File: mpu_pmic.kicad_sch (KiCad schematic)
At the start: 48 parts, among them U501 STPMIC1DPQR

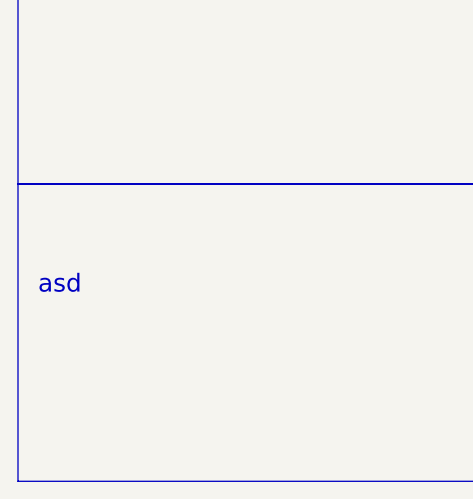
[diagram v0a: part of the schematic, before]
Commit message: Add MPU boot selection
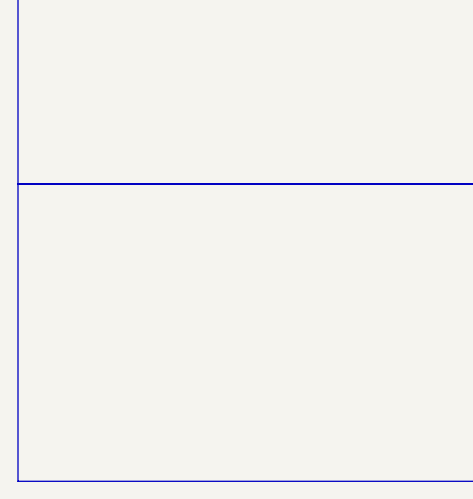
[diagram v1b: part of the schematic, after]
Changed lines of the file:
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@@
-		)
-	)
-	(text_box "asd"
-		(exclude_from_sim no)
-		(at 13.97 260.35 0)
-		(size 283.21 22.86)
-		(margins 0.9525 0.9525 0.9525 0.9525)
-		(stroke
-			(width -0.0001)
-			(type solid)
-		)
-		(fill
-			(type none)
-		)
-		(effects
-			(font
-				(size 2 2)
-			)
-			(justify left top)
 		)
 	)

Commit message: Add a debug section
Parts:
- added R501: 10 kΩ, perfect_footprints:R_0402_1005Metric, symbol Device:R
- renumbered R501 to R502, R502 to R503
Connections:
- net RST_N: now also R501.2
- net V_3V3: now also R501.1
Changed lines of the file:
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@@
 	)
 	(junction
+		(at 97.79 200.66)
+		(diameter 0)
+		(color 0 0 0 0)
+	)
+	(junction
 		(at 349.25 152.4)
 		(diameter 0)
@@
 	)
 	(junction
+		(at 97.79 176.53)
+		(diameter 0)
+		(color 0 0 0 0)
+	)
+	(junction
 		(at 142.24 149.86)
 		(diameter 0)
@@
 	)
 	(bus_entry
-		(at 99.06 203.2)
+		(at 91.44 203.2)
 		(size -2.54 -2.54)
 		(stroke
@@
 	)
 	(bus_entry
-		(at 99.06 195.58)
+		(at 91.44 195.58)
 		(size -2.54 -2.54)
 		(stroke
@@
 	)
 	(bus_entry
-		(at 99.06 205.74)
+		(at 91.44 205.74)
 		(size -2.54 -2.54)
 		(stroke
@@
 	)
 	(bus_entry
-		(at 99.06 193.04)
+		(at 91.44 193.04)
 		(size -2.54 -2.54)
 		(stroke
@@
 	)
 	(bus_entry
-		(at 99.06 200.66)
+		(at 91.44 200.66)
 		(size -2.54 -2.54)
 		(stroke
@@
 	)
 	(bus_entry
-		(at 99.06 198.12)
+		(at 91.44 198.12)
 		(size -2.54 -2.54)
 		(stroke
@@
 	(wire
 		(pts
-			(xy 102.87 176.53) (xy 109.22 176.53)
+			(xy 88.9 176.53) (xy 97.79 176.53)
 		)
 		(stroke
@@
 	(wire
 		(pts
+			(xy 97.79 176.53) (xy 109.22 176.53)
+		)
+		(stroke
+			(width 0)
+			(type default)
+		)
+	)
+	(wire
+		(pts
 			(xy 116.84 125.73) (xy 104.14 125.73)
 		)
@@
 	(bus
 		(pts
-			(xy 95.25 190.5) (xy 96.52 190.5)
+			(xy 87.63 190.5) (xy 88.9 190.5)
 		)
 		(stroke
@@
 	(wire
 		(pts
-			(xy 99.06 198.12) (xy 124.46 198.12)
+			(xy 91.44 198.12) (xy 124.46 198.12)
 		)
 		(stroke
@@
 	(wire
 		(pts
-			(xy 99.06 195.58) (xy 109.22 195.58)
+			(xy 91.44 195.58) (xy 109.22 195.58)
 		)
 		(stroke
@@
 	(wire
 		(pts
+			(xy 97.79 176.53) (xy 97.79 179.07)
+		)
+		(stroke
+			(width 0)
+			(type default)
+		)
+	)
+	(wire
+		(pts
 			(xy 109.22 176.53) (xy 121.92 176.53)
 		)
@@
 	(wire
 		(pts
-			(xy 99.06 205.74) (xy 101.6 205.74)
+			(xy 91.44 205.74) (xy 101.6 205.74)
 		)
 		(stroke
@@
 	(bus
 		(pts
-			(xy 96.52 198.12) (xy 96.52 195.58)
+			(xy 88.9 198.12) (xy 88.9 195.58)
 		)
 		(stroke
@@
 	(bus
 		(pts
-			(xy 96.52 200.66) (xy 96.52 198.12)
+			(xy 88.9 200.66) (xy 88.9 198.12)
 		)
 		(stroke
@@
 	(bus
 		(pts
-			(xy 96.52 193.04) (xy 96.52 195.58)
+			(xy 88.9 193.04) (xy 88.9 195.58)
 		)
 		(stroke
@@
 	(wire
 		(pts
-			(xy 99.06 200.66) (xy 116.84 200.66)
+			(xy 91.44 200.66) (xy 97.79 200.66)
 		)
 		(stroke
@@
 	(bus
 		(pts
-			(xy 96.52 203.2) (xy 96.52 200.66)
+			(xy 88.9 203.2) (xy 88.9 200.66)
 		)
 		(stroke
@@
 	(bus
 		(pts
-			(xy 96.52 193.04) (xy 96.52 190.5)
+			(xy 88.9 193.04) (xy 88.9 190.5)
 		)
 		(stroke
@@
 	(wire
 		(pts
-			(xy 99.06 203.2) (xy 109.22 203.2)
+			(xy 91.44 203.2) (xy 109.22 203.2)
 		)
 		(stroke
@@
 	(wire
 		(pts
-			(xy 99.06 193.04) (xy 121.92 193.04)
+			(xy 91.44 193.04) (xy 121.92 193.04)
 		)
 		(stroke
@@
 	(wire
 		(pts
+			(xy 97.79 200.66) (xy 116.84 200.66)
+		)
+		(stroke
+			(width 0)
+			(type default)
+		)
+	)
+	(wire
+		(pts
 			(xy 336.55 240.03) (xy 339.09 240.03)
 		)
@@
 	(wire
 		(pts
+			(xy 97.79 186.69) (xy 97.79 200.66)
+		)
+		(stroke
+			(width 0)
+			(type default)
+		)
+	)
+	(wire
+		(pts
 			(xy 302.26 166.37) (xy 302.26 165.1)
 		)
@@
 	(hierarchical_label "V_3V3"
 		(shape input)
-		(at 102.87 176.53 180)
+		(at 88.9 176.53 180)
 		(effects
 			(font
@@
 	(hierarchical_label "{PMIC}"
 		(shape bidirectional)
-		(at 95.25 190.5 180)
+		(at 87.63 190.5 180)
 		(effects
 			(font
@@
 		(on_board yes)
 		(dnp no)
-		(property "Reference" "R502"
+		(property "Reference" "R503"
 			(at 124.46 181.6099 0)
 			(effects
@@
 			(project "linux-sbc"
 				(path "/fa11a02f-8043-4153-ab69-88d766503017/2d01087b-54dc-4f43-9cc7-a0ba17201776/8c2fc621-bdce-4f4c-8cac-9098b808a2b8"
-					(reference "R502")
+					(reference "R503")
 					(unit 1)
 				)
@@
 	)
 	(symbol
+		(lib_id "Device:R")
+		(at 97.79 182.88 0)
+		(unit 1)
+		(exclude_from_sim no)
+		(in_bom yes)
+		(on_board yes)
+		(dnp no)
+		(property "Reference" "R501"
+			(at 100.33 181.6099 0)
+			(effects
+				(font
+					(size 1.27 1.27)
+				)
+				(justify left)
+			)
+		)
+		(property "Value" "10 kΩ"
+			(at 100.33 184.1499 0)
+			(effects
+				(font
+					(size 1.27 1.27)
+				)
+				(justify left)
+			)
+		)
+		(property "Footprint" "perfect_footprints:R_0402_1005Metric"
+			(at 96.012 182.88 90)
+			(effects
+				(font
+					(size 1.27 1.27)
+				)
+				(hide yes)
+			)
+		)
+		(property "Datasheet" "https://www.we-online.com/components/products/datasheet/560112110020.pdf"
+			(at 97.79 182.88 0)
+			(effects
+				(font
+					(size 1.27 1.27)
+				)
+				(hide yes)
+			)
+		)
+		(property "Description" "Resistor"
+			(at 97.79 182.88 0)
+			(effects
+				(font
+					(size 1.27 1.27)
+				)
+				(hide yes)
+			)
+		)
+		(property "DigiKey Part Number" "732-560112110020CT-ND"
+			(at 97.79 182.88 0)
+			(effects
+				(font
+					(size 1.27 1.27)
+				)
+				(hide yes)
+			)
+		)
+		(property "MPN" "560112110020"
+			(at 97.79 182.88 0)
+			(effects
+				(font
+					(size 1.27 1.27)
+				)
+				(hide yes)
+			)
+		)
+		(property "Manufacturer" "Würth Elektronik"
+			(at 97.79 182.88 0)
+			(effects
+				(font
+					(size 1.27 1.27)
+				)
+				(hide yes)
+			)
+		)
+		(property "Temperature Coefficient" ""
+			(at 97.79 182.88 0)
+			(effects
+				(font
+					(size 1.27 1.27)
+				)
+				(hide yes)
+			)
+		)
+		(pin "2"
+		)
+		(pin "1"
+		)
+		(instances
+			(project "linux-sbc"
+				(path "/fa11a02f-8043-4153-ab69-88d766503017/2d01087b-54dc-4f43-9cc7-a0ba17201776/8c2fc621-bdce-4f4c-8cac-9098b808a2b8"
+					(reference "R501")
+					(unit 1)
+				)
+			)
+		)
+	)
+	(symbol
 		(lib_id "STMicroelectronics:STPMIC1DPQR")
 		(at 182.88 160.02 0)
@@
 		(on_board yes)
 		(dnp no)
-		(property "Reference" "R501"
+		(property "Reference" "R502"
 			(at 111.76 181.6099 0)
 			(effects
@@
 			(project "linux-sbc"
 				(path "/fa11a02f-8043-4153-ab69-88d766503017/2d01087b-54dc-4f43-9cc7-a0ba17201776/8c2fc621-bdce-4f4c-8cac-9098b808a2b8"
-					(reference "R501")
+					(reference "R502")
 					(unit 1)
 				)

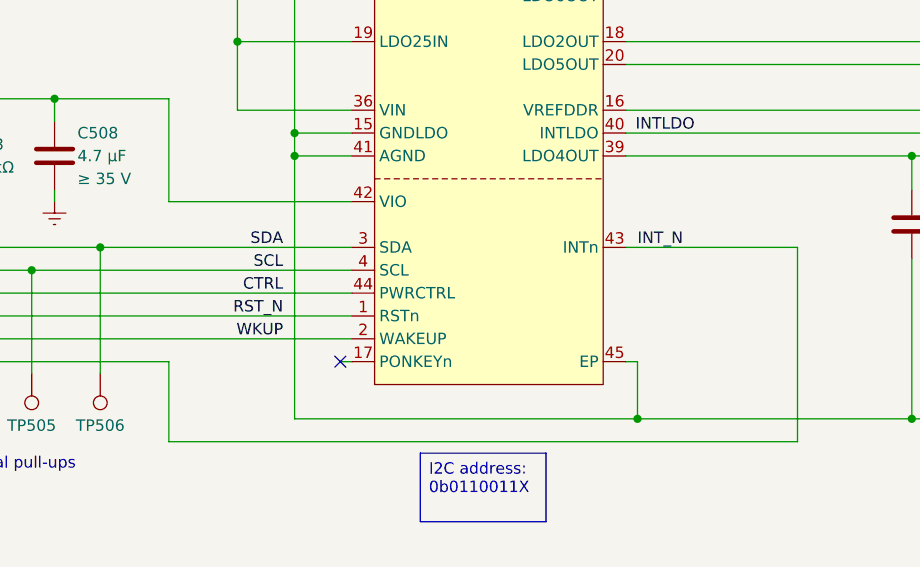
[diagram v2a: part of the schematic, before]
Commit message: Add ETH schema
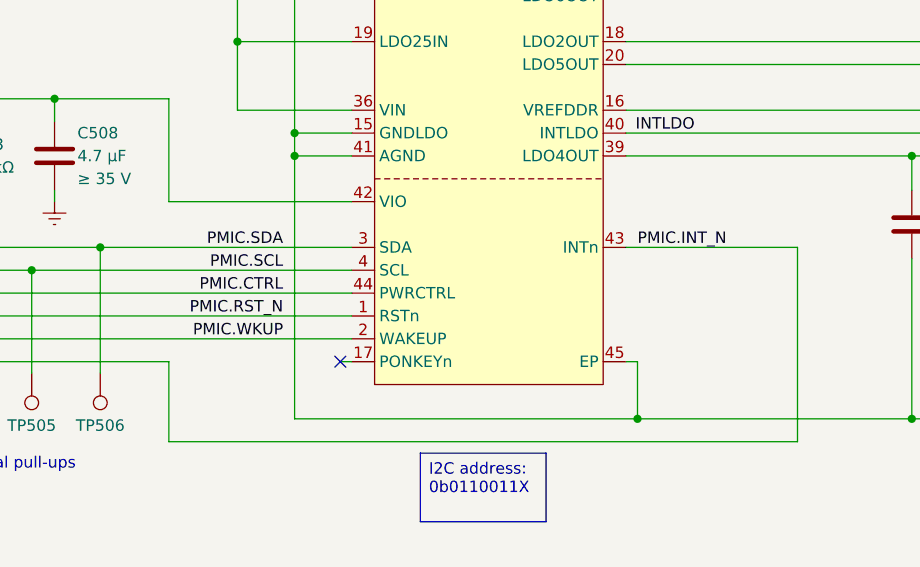
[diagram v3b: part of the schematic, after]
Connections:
- net CTRL renamed PMIC.CTRL
- net INT_N renamed PMIC.INT_N
- net RST_N renamed PMIC.RST_N
- net SCL renamed PMIC.SCL
- net SDA renamed PMIC.SDA
- net WKUP renamed PMIC.WKUP
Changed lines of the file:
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@@
 	)
 	(bus_alias "PMIC"
-		(members "SDA" "SCL" "CTRL" "RST_N" "WKUP" "INT_N")
+		(members "PMIC.SDA" "PMIC.SCL" "PMIC.CTRL" "PMIC.RST_N" "PMIC.WKUP" "PMIC.INT_N")
 	)
 	(text "RST_N & INT_N have internal pull-ups"
@@
 		)
 	)
-	(label "SCL"
+	(label "PMIC.SCL"
 		(at 160.02 195.58 180)
 		(effects
@@
 		)
 	)
-	(label "INT_N"
+	(label "PMIC.INT_N"
 		(at 199.39 193.04 0)
 		(effects
@@
 		)
 	)
-	(label "SDA"
+	(label "PMIC.SDA"
 		(at 160.02 193.04 180)
 		(effects
@@
 		)
 	)
-	(label "CTRL"
+	(label "PMIC.CTRL"
 		(at 160.02 198.12 180)
 		(effects
@@
 		)
 	)
-	(label "WKUP"
+	(label "PMIC.WKUP"
 		(at 160.02 203.2 180)
 		(effects
@@
 		)
 	)
-	(label "RST_N"
+	(label "PMIC.RST_N"
 		(at 160.02 200.66 180)
 		(effects

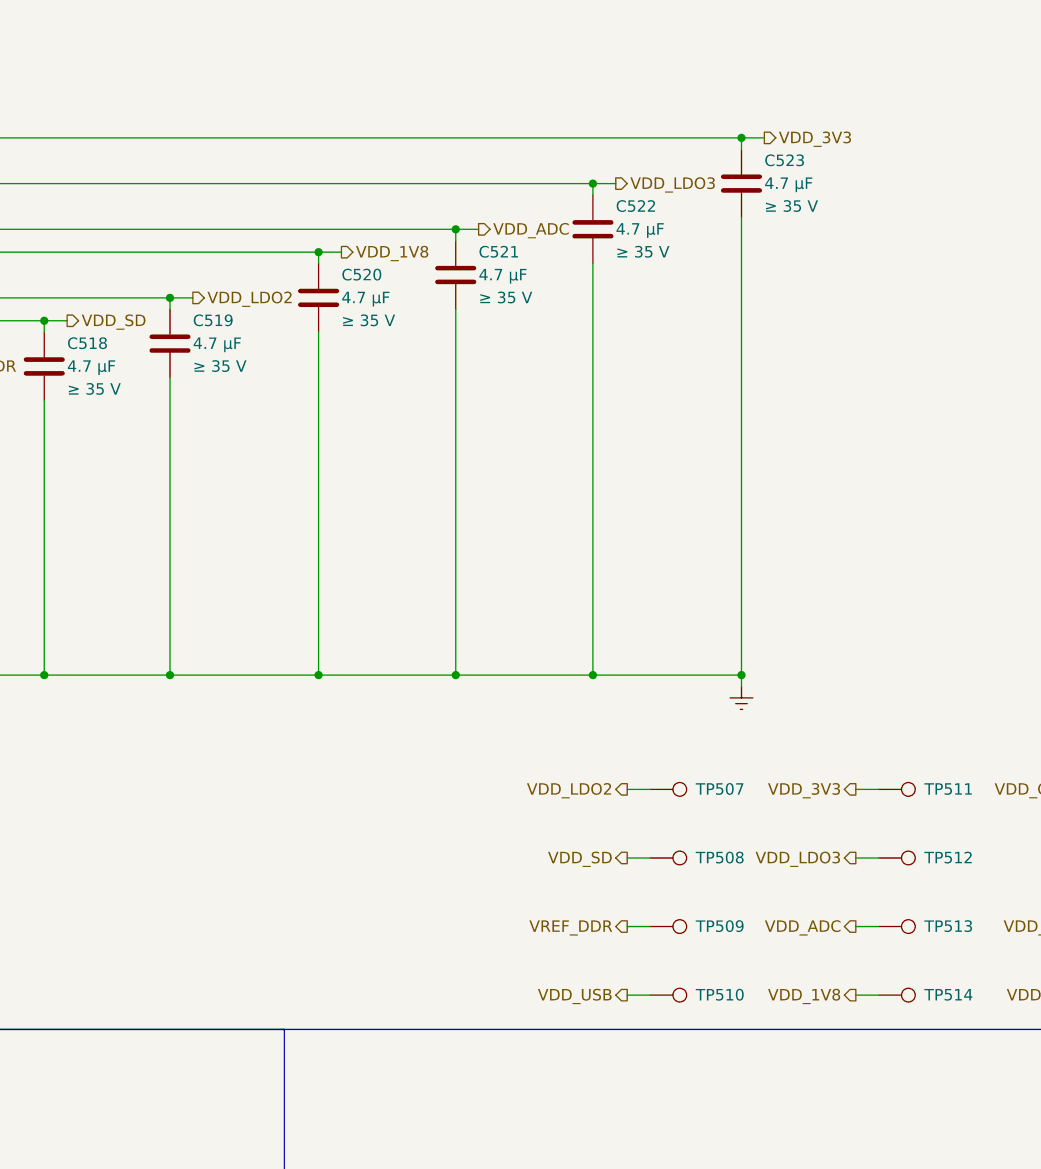
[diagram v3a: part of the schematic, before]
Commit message: Add LCD screen
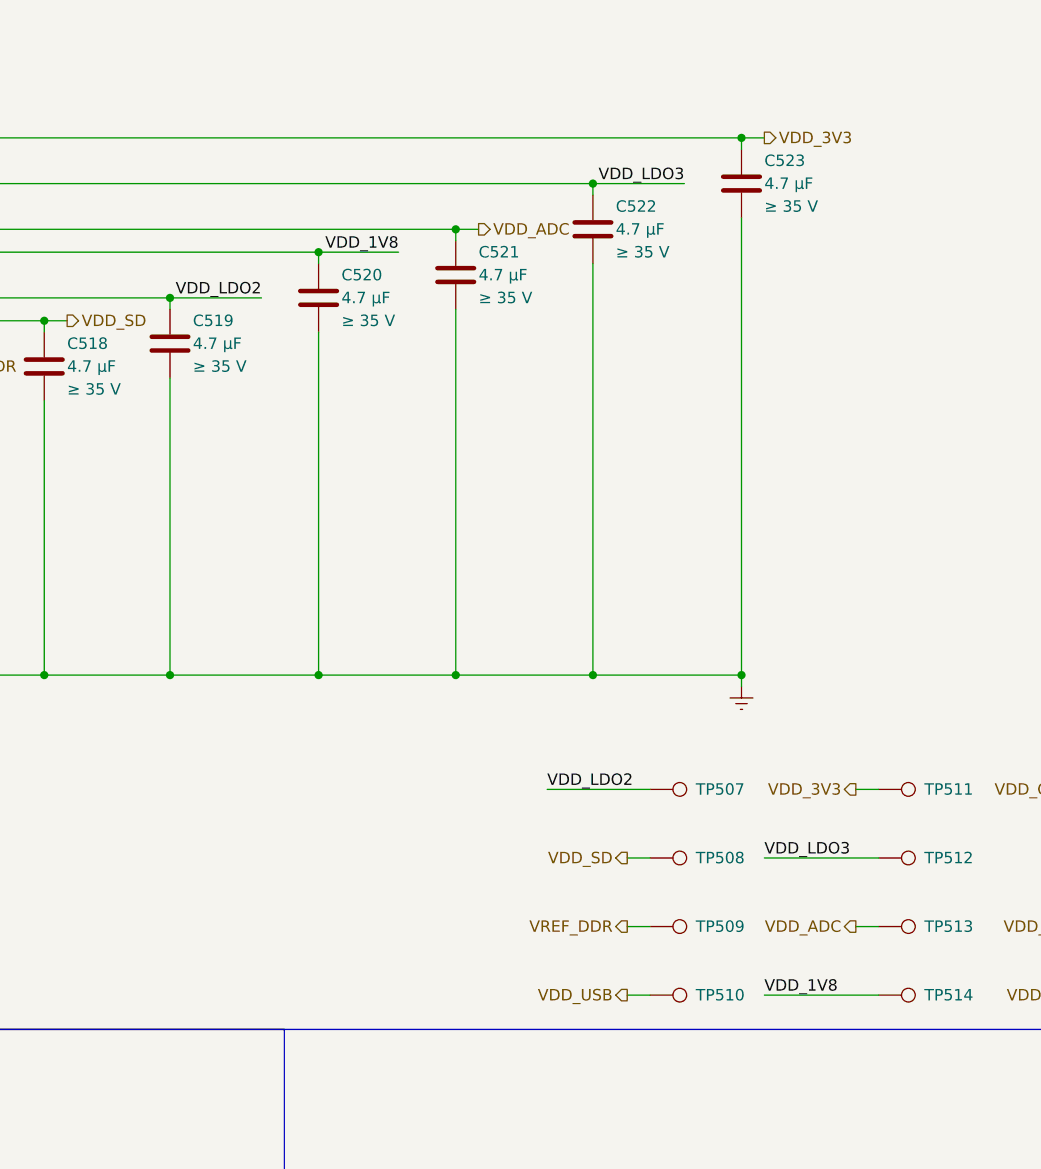
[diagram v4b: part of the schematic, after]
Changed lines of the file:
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@@
 	(wire
 		(pts
-			(xy 285.75 170.18) (xy 288.29 170.18)
+			(xy 285.75 170.18) (xy 295.91 170.18)
 		)
 		(stroke
@@
 	(wire
 		(pts
-			(xy 332.74 157.48) (xy 335.28 157.48)
+			(xy 332.74 157.48) (xy 342.9 157.48)
 		)
 		(stroke
@@
 	(wire
 		(pts
-			(xy 302.26 165.1) (xy 304.8 165.1)
+			(xy 302.26 165.1) (xy 311.15 165.1)
 		)
 		(stroke
@@
 	(wire
 		(pts
-			(xy 361.95 232.41) (xy 364.49 232.41)
+			(xy 351.79 232.41) (xy 364.49 232.41)
 		)
 		(stroke
@@
 	(wire
 		(pts
-			(xy 336.55 224.79) (xy 339.09 224.79)
+			(xy 327.66 224.79) (xy 339.09 224.79)
 		)
 		(stroke
@@
 	(wire
 		(pts
-			(xy 361.95 247.65) (xy 364.49 247.65)
+			(xy 351.79 247.65) (xy 364.49 247.65)
 		)
 		(stroke
@@
 			(width 0)
 			(type default)
+		)
+	)
+	(label "VDD_LDO3"
+		(at 342.9 157.48 180)
+		(effects
+			(font
+				(size 1.27 1.27)
+			)
+			(justify right bottom)
+		)
+	)
+	(label "VDD_1V8"
+		(at 351.79 247.65 0)
+		(effects
+			(font
+				(size 1.27 1.27)
+			)
+			(justify left bottom)
+		)
+	)
+	(label "VDD_1V8"
+		(at 311.15 165.1 180)
+		(effects
+			(font
+				(size 1.27 1.27)
+			)
+			(justify right bottom)
+		)
+	)
+	(label "VDD_LDO3"
+		(at 351.79 232.41 0)
+		(effects
+			(font
+				(size 1.27 1.27)
+			)
+			(justify left bottom)
 		)
 	)
@@
 		)
 	)
+	(label "VDD_LDO2"
+		(at 295.91 170.18 180)
+		(effects
+			(font
+				(size 1.27 1.27)
+			)
+			(justify right bottom)
+		)
+	)
 	(label "PMIC.SDA"
 		(at 160.02 193.04 180)
@@
 		)
 	)
+	(label "VDD_LDO2"
+		(at 327.66 224.79 0)
+		(effects
+			(font
+				(size 1.27 1.27)
+			)
+			(justify left bottom)
+		)
+	)
 	(label "PMIC.CTRL"
 		(at 160.02 198.12 180)
@@
 			)
 			(justify right bottom)
-		)
-	)
-	(hierarchical_label "VDD_LDO2"
-		(shape output)
-		(at 288.29 170.18 0)
-		(effects
-			(font
-				(size 1.27 1.27)
-			)
-			(justify left)
 		)
 	)
@@
 		)
 	)
-	(hierarchical_label "VDD_LDO3"
-		(shape output)
-		(at 335.28 157.48 0)
-		(effects
-			(font
-				(size 1.27 1.27)
-			)
-			(justify left)
-		)
-	)
 	(hierarchical_label "VDD_USB"
 		(shape output)
@@
 		)
 	)
-	(hierarchical_label "VDD_LDO3"
-		(shape output)
-		(at 361.95 232.41 180)
-		(effects
-			(font
-				(size 1.27 1.27)
-			)
-			(justify right)
-		)
-	)
 	(hierarchical_label "VDD_DDR"
 		(shape output)
@@
 		)
 	)
-	(hierarchical_label "VDD_1V8"
-		(shape output)
-		(at 361.95 247.65 180)
-		(effects
-			(font
-				(size 1.27 1.27)
-			)
-			(justify right)
-		)
-	)
 	(hierarchical_label "VDD_DDR"
 		(shape output)
@@
 		)
 	)
-	(hierarchical_label "VDD_LDO2"
-		(shape output)
-		(at 336.55 224.79 180)
-		(effects
-			(font
-				(size 1.27 1.27)
-			)
-			(justify right)
-		)
-	)
 	(hierarchical_label "VDD_ADC"
 		(shape output)
@@
 		)
 	)
-	(hierarchical_label "VDD_1V8"
-		(shape output)
-		(at 304.8 165.1 0)
-		(effects
-			(font
-				(size 1.27 1.27)
-			)
-			(justify left)
-		)
-	)
